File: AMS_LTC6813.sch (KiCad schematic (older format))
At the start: 69 parts, among them J1 CELLVOLCON, J10 Conn_01x02_Male, J11 Conn_01x02_Male, J12 Conn_01x02_Male, J13 Conn_01x02_Male, J14 Conn_01x02_Male, J15 Conn_01x02_Male, J16 Conn_01x02_Male, J17 Conn_01x02_Male, J18 Conn_01x02_Male, J19 Conn_01x02_Male, J2 TEMPSENCON, J20 Conn_01x02_Male, J21 Conn_01x02_Male, J22 Conn_01x02_Male, J23 Conn_01x02_Male, J24 Conn_01x02_Male, J25 Conn_01x02_Male, J26 Conn_01x02_Male, J27 Conn_01x02_Male, J28 Conn_01x02_Male, J29 Conn_01x02_Male, J3 ISOSPI2, J30 Conn_01x02_Male, J31 Conn_01x02_Male, J32 Conn_01x02_Male, J33 Conn_01x02_Male, J34 Conn_01x02_Male, J35 Conn_01x02_Male, J36 Conn_01x02_Male, J37 Conn_01x02_Male, J38 Conn_01x02_Male, J39 Conn_01x02_Male, J4 ISOSPI1, J40 Conn_01x02_Male, J41 Conn_01x02_Male, J42 Conn_01x02_Male, J43 Conn_01x02_Male, J44 Conn_01x02_Male, J45 Conn_01x02_Male, J46 Conn_01x02_Male, J47 Conn_01x02_Male, J48 Conn_01x02_Male, J49 Conn_01x02_Male, J5 Conn_01x02_Male, J50 Conn_01x02_Male, J51 Conn_01x02_Male, J52 Conn_01x02_Male, J53 Conn_01x02_Male, J54 Conn_01x02_Male, J55 Conn_01x02_Male, J56 Conn_01x02_Male, J57 Conn_01x02_Male, J58 Conn_01x02_Male, J59 Conn_01x02_Male, J6 Conn_01x02_Male, J60 Conn_01x02_Male, J61 Conn_01x02_Male, J62 Conn_01x02_Male, J63 Conn_01x02_Male, J64 Conn_01x02_Male, J65 Conn_01x02_Male, J66 Conn_01x02_Male, J67 Conn_01x02_Male, J68 Conn_01x02_Male, J7 Conn_01x02_Male, J8 Conn_01x02_Male, J9 Conn_01x02_Male, U2 LTC6813-1

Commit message: adding com
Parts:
- removed J1: CELLVOLCON, AMS_custom_lib:VOLCELLCON, symbol AMS_custom_lib:CELLVOLCON
- removed J2: TEMPSENCON, AMS_custom_lib:TEMPSENSCON, symbol AMS_custom_lib:TEMPSENCON
- removed J3: ISOSPI2, AMS_custom_lib:ISOSPICON, symbol AMS_custom_lib:ISOSPI2
- removed J4: ISOSPI1, AMS_custom_lib:ISOSPICON, symbol AMS_custom_lib:ISOSPI1
- added J?: Conn_02x20_Counter_Clockwise, Connector_IDC:IDC-Header_2x20_P2.54mm_Vertical, symbol Connector_Generic:Conn_02x20_Counter_Clockwise
- added J? (x2): Conn_01x03_Female, Connector_PinHeader_2.54mm:PinHeader_1x03_P2.54mm_Vertical, symbol Connector:Conn_01x03_Female
- added J? (x2): Conn_01x06, Connector_PinHeader_2.54mm:PinHeader_1x06_P2.54mm_Vertical, symbol Connector_Generic:Conn_01x06
- added J? (x2): Conn_02x02_Counter_Clockwise, Connector_PinHeader_2.54mm:PinHeader_2x02_P2.54mm_Vertical, symbol Connector_Generic:Conn_02x02_Counter_Clockwise
- added R?: 100, Resistor_SMD:R_1206_3216Metric_Pad1.42x1.75mm_HandSolder, symbol Device:R
- added R?: 5k, Resistor_SMD:R_1206_3216Metric_Pad1.42x1.75mm_HandSolder, symbol Device:R
- added U?: LTC6820, Package_SO:MSOP-16_3x4mm_P0.5mm, symbol AMS_custom_lib:LTC6820
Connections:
- net V- is gone; now on net C0: J63.1 (Pin_1), J63.2 (Pin_2), J64.1 (Pin_1), J64.2 (Pin_2), U2.59 (V-), U2.60 (V-)
- net C0: now also J?.2 (Pin_2), J?.20 (Pin_20), J?.3 (Pin_3), J?.5 (Pin_5), U?.14 (GND)
- net CELL1: now also J?.19 (Pin_19)
- net CELL10: now also J?.10 (Pin_10)
- net CELL11: now also J?.9 (Pin_9)
- net CELL12: now also J?.8 (Pin_8)
- net CELL2: now also J?.18 (Pin_18)
- net CELL3: now also J?.17 (Pin_17)
- net CELL4: now also J?.16 (Pin_16)
- net CELL5: now also J?.15 (Pin_15)
- net CELL6: now also J?.14 (Pin_14)
- net CELL7: now also J?.13 (Pin_13)
- net CELL8: now also J?.12 (Pin_12)
- net CELL9: now also J?.11 (Pin_11)
- net CSBIMA: now also J?.2 (Pin_2), J?.2 (Pin_2)
- net GPIO1: now also J?.21 (Pin_21)
- net GPIO2: now also J?.22 (Pin_22)
- net GPIO3: now also J?.23 (Pin_23)
- net GPIO4: now also J?.24 (Pin_24)
- net GPIO5: now also J?.25 (Pin_25)
- net GPIO6: now also J?.26 (Pin_26)
- net GPIO7: now also J?.27 (Pin_27)
- net GPIO8: now also J?.28 (Pin_28)
- net GPIO9: now also J?.29 (Pin_29)
- net IBIAS: now also J?.1 (Pin_1)
- net IMB: now also R?.1
- net IPB: now also R?.2
- net SCKIPA: now also J?.1 (Pin_1), J?.1 (Pin_1)
- net SDI: now also J?.4 (Pin_4)
- net SDO: now also J?.3 (Pin_3), R?.1
- new net CELL13: J?.7 (Pin_7)
- new net CELL14: J?.6 (Pin_6)
- new net CELL15: J?.5 (Pin_5)
- new net CELL16: J?.4 (Pin_4)
- new net CELL17: J?.3 (Pin_3)
- new net CELL18: J?.2 (Pin_2)
- new net CS: J?.5 (Pin_5), U?.5 (~CS)
- new net CSBIMA1: J?.2 (Pin_2), J?.3 (Pin_3)
- new net GND1: J?.3 (Pin_3)
- new net IBIAS1: J?.1 (Pin_1), U?.16 (IBIAS)
- new net ICMB: J?.2 (Pin_2)
- new net ICMB1: J?.2 (Pin_2)
- new net ICMP1: U?.15 (ICMP)
- new net IM: J?.3 (Pin_3), U?.10 (IM)
- new net IP: J?.4 (Pin_4), U?.11 (ID)
- new net MISO: J?.4 (Pin_4), U?.3 (MISO)
- new net MOSI: J?.3 (Pin_3), U?.2 (MOSI)
- new net SCK: U?.4 (SCK)
- new net SCKIPA1: J?.1 (Pin_1), J?.4 (Pin_4)
- new net SCk: J?.6 (Pin_6)
- new net VDD1: J?.1 (Pin_1), U?.12 (MSTR), U?.6 (Vdds), U?.7 (POL), U?.8 (PMD), U?.9 (Vdd)
- new net VDD2: J?.6 (Pin_6), R?.2

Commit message: blabl
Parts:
- added C? (x3): 1u, Capacitor_SMD:C_1210_3225Metric_Pad1.42x2.65mm_HandSolder, symbol Device:C
- added C?: 0.1u, Capacitor_SMD:C_1210_3225Metric_Pad1.42x2.65mm_HandSolder, symbol Device:C
- added Q?: 2N2219, Package_TO_SOT_THT:TO-39-3, symbol Transistor_BJT:2N2219
- added R?: R, Resistor_SMD:R_1206_3216Metric_Pad1.42x1.75mm_HandSolder, symbol Device:R
- gave numbers to parts that had none: 10
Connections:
- net C0: now also C?.2, C?.2, C?.2, C?.2
- net C18: now also R?.1
- net DRIVE: now also Q?.2 (B)
- net VREF1: now also C?.1
- net VREF2: now also C?.1
- net VREG: now also C?.1, Q?.1 (E)
- new net C: C?.1, Q?.3 (C), R?.2
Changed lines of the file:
@@
 CELL18
 $Comp
-L Connector_Generic:Conn_02x20_Counter_Clockwise J?
+L Connector_Generic:Conn_02x20_Counter_Clockwise J71
 U 1 1 5F95EEEE
 P 9400 1700
-F 0 "J?" H 9450 2817 50  0000 C CNN
+F 0 "J71" H 9450 2817 50  0000 C CNN
 F 1 "Conn_02x20_Counter_Clockwise" H 9450 2726 50  0000 C CNN
 F 2 "Connector_IDC:IDC-Header_2x20_P2.54mm_Vertical" H 9400 1700 50  0001 C CNN
@@
 GPIO9
 $Comp
-L Device:R R?
+L Device:R R73
 U 1 1 5F96165A
 P 4600 6250
-F 0 "R?" V 4393 6250 50  0000 C CNN
+F 0 "R73" V 4393 6250 50  0000 C CNN
 F 1 "100" V 4484 6250 50  0000 C CNN
 F 2 "Resistor_SMD:R_1206_3216Metric_Pad1.42x1.75mm_HandSolder" V 4530 6250 50  0001 C CNN
@@
 CSBIMA1
 $Comp
-L Connector_Generic:Conn_01x06 J?
+L Connector_Generic:Conn_01x06 J3
 U 1 1 5F963338
 P 5850 5200
-F 0 "J?" H 5930 5192 50  0000 L CNN
+F 0 "J3" H 5930 5192 50  0000 L CNN
 F 1 "Conn_01x06" H 5930 5101 50  0000 L CNN
 F 2 "Connector_PinHeader_2.54mm:PinHeader_1x06_P2.54mm_Vertical" H 5850 5200 50  0001 C CNN
@@
 VDD2
 $Comp
-L Device:R R?
+L Device:R R74
 U 1 1 5F963D26
 P 5350 5350
-F 0 "R?" H 5420 5396 50  0000 L CNN
+F 0 "R74" H 5420 5396 50  0000 L CNN
 F 1 "5k" H 5420 5305 50  0000 L CNN
 F 2 "Resistor_SMD:R_1206_3216Metric_Pad1.42x1.75mm_HandSolder" V 5280 5350 50  0001 C CNN
@@
 Connection ~ 5350 5500
 $Comp
-L AMS_custom_lib:LTC6820 U?
+L AMS_custom_lib:LTC6820 U1
 U 1 1 5F9642E1
 P 6000 7000
-F 0 "U?" H 5975 7615 50  0000 C CNN
+F 0 "U1" H 5975 7615 50  0000 C CNN
 F 1 "LTC6820" H 5975 7524 50  0000 C CNN
 F 2 "Package_SO:MSOP-16_3x4mm_P0.5mm" H 5950 7500 50  0001 C CNN
@@
 $EndComp
 $Comp
-L Connector_Generic:Conn_01x06 J?
+L Connector_Generic:Conn_01x06 J1
 U 1 1 5F9647DF
 P 4550 7050
-F 0 "J?" H 4470 6525 50  0000 C CNN
+F 0 "J1" H 4470 6525 50  0000 C CNN
 F 1 "Conn_01x06" H 4470 6616 50  0000 C CNN
 F 2 "Connector_PinHeader_2.54mm:PinHeader_1x06_P2.54mm_Vertical" H 4550 7050 50  0001 C CNN
@@
 VDD1
 $Comp
-L Connector_Generic:Conn_02x02_Counter_Clockwise J?
+L Connector_Generic:Conn_02x02_Counter_Clockwise J69
 U 1 1 5F96687F
 P 7100 5300
-F 0 "J?" H 7150 5517 50  0000 C CNN
+F 0 "J69" H 7150 5517 50  0000 C CNN
 F 1 "Conn_02x02_Counter_Clockwise" H 7150 5426 50  0000 C CNN
 F 2 "Connector_PinHeader_2.54mm:PinHeader_2x02_P2.54mm_Vertical" H 7100 5300 50  0001 C CNN
@@
 CSBIMA
 $Comp
-L Connector_Generic:Conn_02x02_Counter_Clockwise J?
+L Connector_Generic:Conn_02x02_Counter_Clockwise J4
 U 1 1 5F967148
 P 6450 6000
-F 0 "J?" H 6500 6217 50  0000 C CNN
+F 0 "J4" H 6500 6217 50  0000 C CNN
 F 1 "Conn_02x02_Counter_Clockwise" H 6500 6126 50  0000 C CNN
 F 2 "Connector_PinHeader_2.54mm:PinHeader_2x02_P2.54mm_Vertical" H 6450 6000 50  0001 C CNN
@@
 GND
 $Comp
-L Connector:Conn_01x03_Female J?
+L Connector:Conn_01x03_Female J2
 U 1 1 5F962EA3
 P 4750 5650
-F 0 "J?" H 4777 5676 50  0000 L CNN
+F 0 "J2" H 4777 5676 50  0000 L CNN
 F 1 "Conn_01x03_Female" H 4777 5585 50  0000 L CNN
 F 2 "Connector_PinHeader_2.54mm:PinHeader_1x03_P2.54mm_Vertical" H 4750 5650 50  0001 C CNN
@@
 $EndComp
 $Comp
-L Connector:Conn_01x03_Female J?
+L Connector:Conn_01x03_Female J70
 U 1 1 5F9677A5
 P 7550 6000
-F 0 "J?" H 7577 6026 50  0000 L CNN
+F 0 "J70" H 7577 6026 50  0000 L CNN
 F 1 "Conn_01x03_Female" H 7577 5935 50  0000 L CNN
 F 2 "Connector_PinHeader_2.54mm:PinHeader_1x03_P2.54mm_Vertical" H 7550 6000 50  0001 C CNN
@@
 Text Label 5550 7350 2    50   ~ 0
 VDD1
+$Comp
+L Device:C C?
+U 1 1 5F96A5E9
+P 9150 5150
+F 0 "C?" H 9265 5196 50  0000 L CNN
+F 1 "1u" H 9265 5105 50  0000 L CNN
+F 2 "Capacitor_SMD:C_1210_3225Metric_Pad1.42x2.65mm_HandSolder" H 9188 5000 50  0001 C CNN
+F 3 "~" H 9150 5150 50  0001 C CNN
+	1    9150 5150
+	1    0    0    -1
+$EndComp
+$Comp
+L Device:C C?
+U 1 1 5F96A6FB
+P 9500 5150
+F 0 "C?" H 9615 5196 50  0000 L CNN
+F 1 "1u" H 9615 5105 50  0000 L CNN
+F 2 "Capacitor_SMD:C_1210_3225Metric_Pad1.42x2.65mm_HandSolder" H 9538 5000 50  0001 C CNN
+F 3 "~" H 9500 5150 50  0001 C CNN
+	1    9500 5150
+	1    0    0    -1
+$EndComp
+$Comp
+L Device:C C?
+U 1 1 5F96A94A
+P 9850 5150
+F 0 "C?" H 9965 5196 50  0000 L CNN
+F 1 "1u" H 9965 5105 50  0000 L CNN
+F 2 "Capacitor_SMD:C_1210_3225Metric_Pad1.42x2.65mm_HandSolder" H 9888 5000 50  0001 C CNN
+F 3 "~" H 9850 5150 50  0001 C CNN
+	1    9850 5150
+	1    0    0    -1
+$EndComp
+$Comp
+L Device:C C?
+U 1 1 5F96AA68
+P 10200 5150
+F 0 "C?" H 10315 5196 50  0000 L CNN
+F 1 "0.1u" H 10315 5105 50  0000 L CNN
+F 2 "Capacitor_SMD:C_1210_3225Metric_Pad1.42x2.65mm_HandSolder" H 10238 5000 50  0001 C CNN
+F 3 "~" H 10200 5150 50  0001 C CNN
+	1    10200 5150
+	1    0    0    -1
+$EndComp
+Text Label 10550 5300 0    50   ~ 0
+GND
+Wire Wire Line
+	10550 5300 10200 5300
+Wire Wire Line
+	10200 5300 9850 5300
+Connection ~ 10200 5300
+Wire Wire Line
+	9850 5300 9500 5300
+Connection ~ 9850 5300
+Wire Wire Line
+	9500 5300 9150 5300
+Connection ~ 9500 5300
+Text Label 9150 5000 0    50   ~ 0
+VREF1
+Text Label 9500 5000 0    50   ~ 0
+VREF2
+Text Label 9850 5000 0    50   ~ 0
+VREG
+$Comp
+L Device:R R?
+U 1 1 5F96B10A
+P 10200 4850
+F 0 "R?" H 10270 4896 50  0000 L CNN
+F 1 "R" H 10270 4805 50  0000 L CNN
+F 2 "Resistor_SMD:R_1206_3216Metric_Pad1.42x1.75mm_HandSolder" V 10130 4850 50  0001 C CNN
+F 3 "~" H 10200 4850 50  0001 C CNN
+	1    10200 4850
+	1    0    0    -1
+$EndComp
+Text Label 10200 4700 0    50   ~ 0
+C18
+Text Label 10200 5000 0    50   ~ 0
+C
+$Comp
+L Transistor_BJT:2N2219 Q?
+U 1 1 5F96B7EA
+P 9900 5900
+F 0 "Q?" H 10091 5946 50  0000 L CNN
+F 1 "2N2219" H 10091 5855 50  0000 L CNN
+F 2 "Package_TO_SOT_THT:TO-39-3" H 10100 5825 50  0001 L CIN
+F 3 "http://www.onsemi.com/pub_link/Collateral/2N2219-D.PDF" H 9900 5900 50  0001 L CNN
+	1    9900 5900
+	1    0    0    -1
+$EndComp
+Text Label 10000 5700 0    50   ~ 0
+C
+Text Label 10000 6100 0    50   ~ 0
+VREG
+Text Label 9700 5900 2    50   ~ 0
+DRIVE
 $EndSCHEMATC

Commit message: petite modif
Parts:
- added J72, J73, J74, J75, J76, J77, J78, J79, J80, J81, J82, J83, J84, J85, J86, J87: Conn_01x02_Male, Connector_PinHeader_2.54mm:PinHeader_1x02_P2.54mm_Vertical, symbol Connector:Conn_01x02_Male
- gave numbers to parts that had none: 6
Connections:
- net C0: now also J82.1 (Pin_1), J82.2 (Pin_2)
- net CS: now also J76.1 (Pin_1), J76.2 (Pin_2)
- net IBIAS1: now also J80.1 (Pin_1), J80.2 (Pin_2)
- net ICMP1: now also J81.1 (Pin_1), J81.2 (Pin_2)
- net IM: now also J86.1 (Pin_1), J86.2 (Pin_2)
- net IP: now also J85.1 (Pin_1), J85.2 (Pin_2)
- net MISO: now also J74.1 (Pin_1), J74.2 (Pin_2)
- net MOSI: now also J73.1 (Pin_1), J73.2 (Pin_2)
- net SCK: now also J75.1 (Pin_1), J75.2 (Pin_2)
- net VDD1: now also J77.1 (Pin_1), J77.2 (Pin_2), J78.1 (Pin_1), J78.2 (Pin_2), J79.1 (Pin_1), J79.2 (Pin_2), J84.1 (Pin_1), J84.2 (Pin_2), J87.1 (Pin_1), J87.2 (Pin_2)
- net EN: now reaches U1.1 (EN)
- net EN: now also J72.1 (Pin_1), J72.2 (Pin_2)
- net SLOW: now reaches U1.13 (SLOW)
- net SLOW: now also J83.1 (Pin_1), J83.2 (Pin_2)
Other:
- moved on the sheet: J1, J2, R73

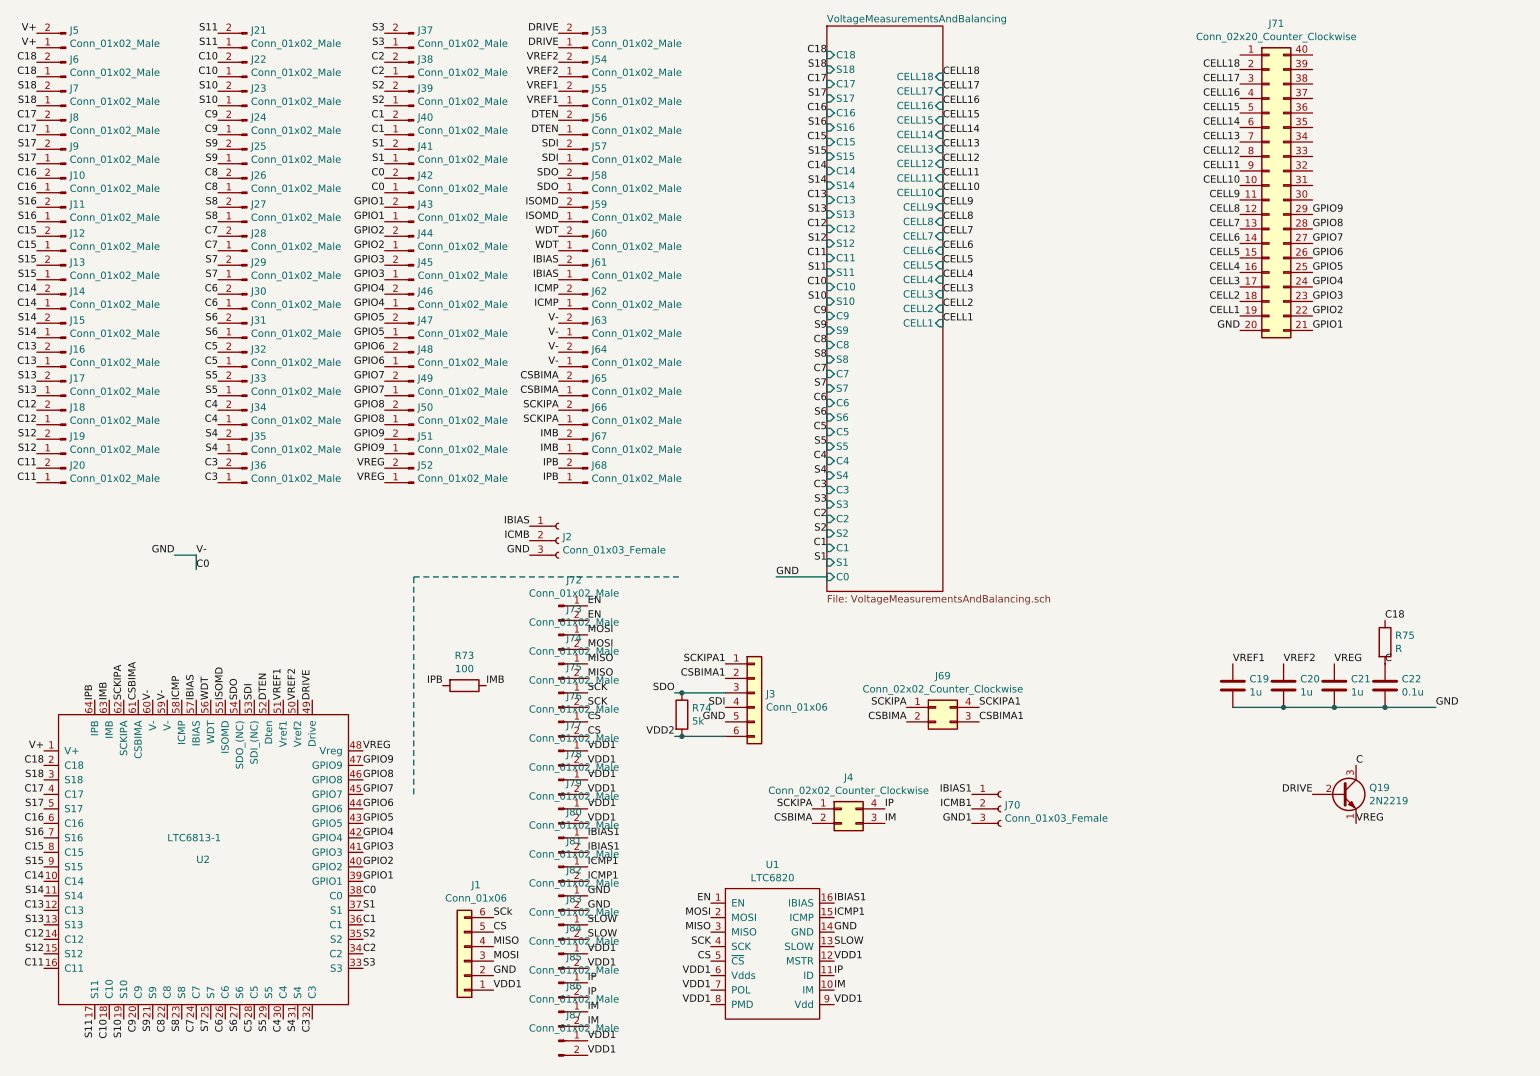
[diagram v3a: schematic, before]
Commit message: tout route sauf voltage channel
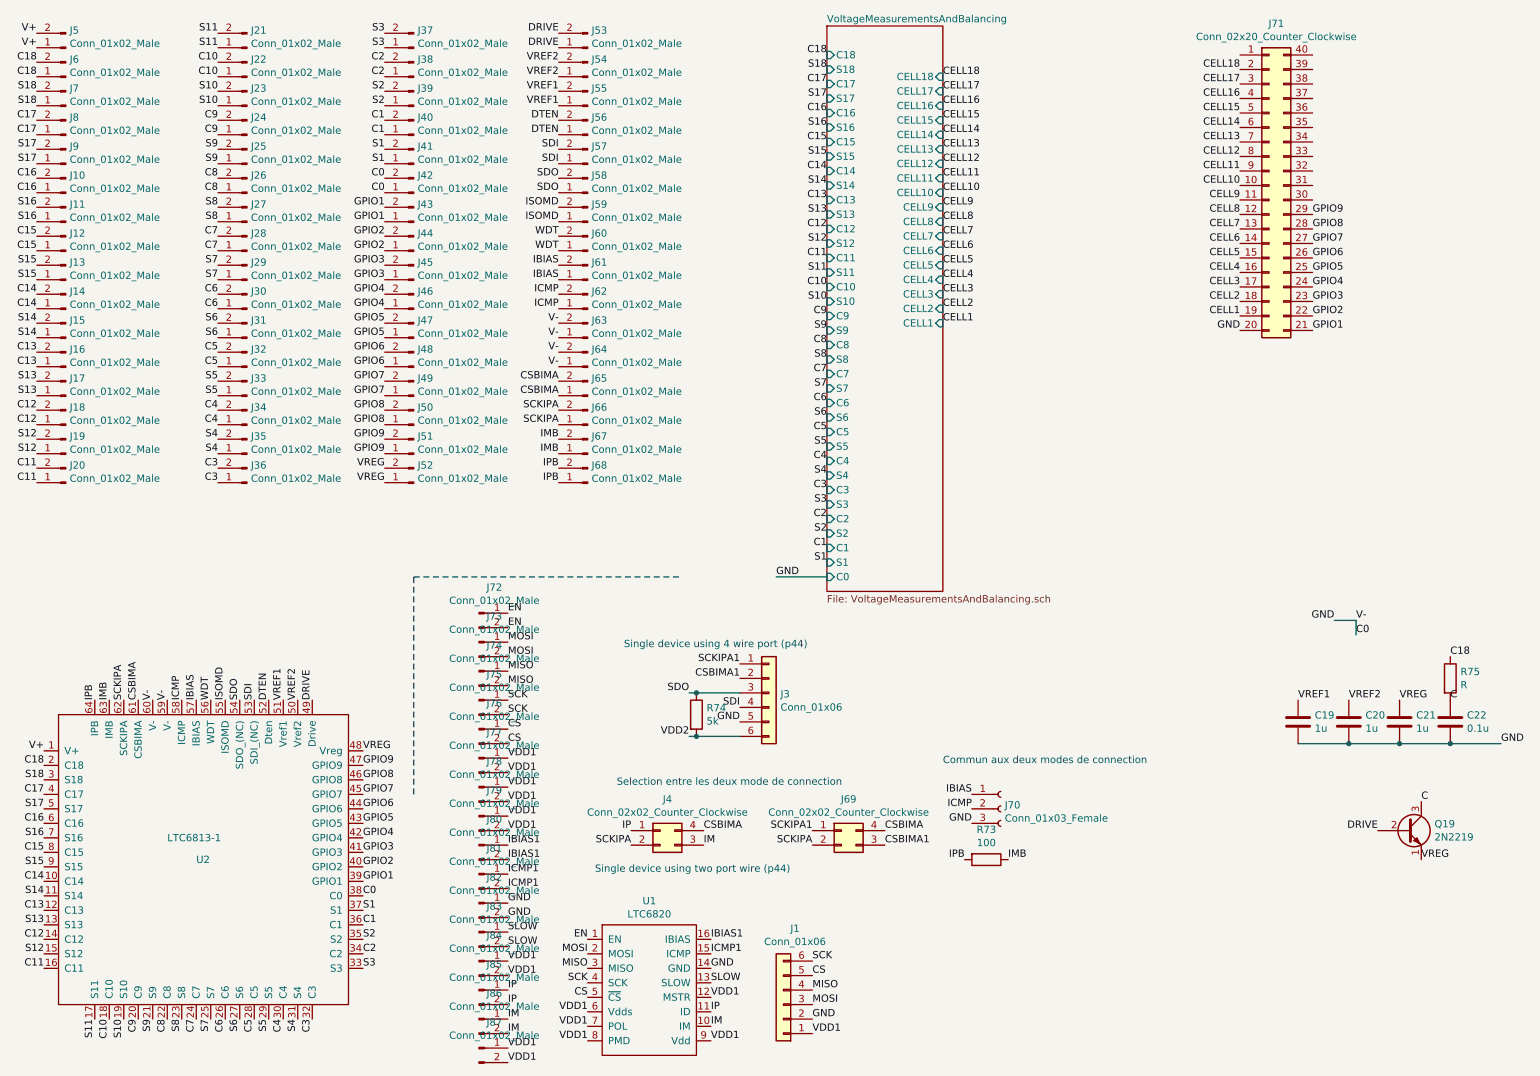
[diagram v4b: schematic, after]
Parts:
- removed J2: Conn_01x03_Female, Connector_PinHeader_2.54mm:PinHeader_1x03_P2.54mm_Vertical, symbol Connector:Conn_01x03_Female
- Q19: footprint Package_TO_SOT_THT:TO-39-3 -> Package_TO_SOT_SMD:SOT-223-3_TabPin2
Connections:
- net GND1 is gone; now on net C0: J70.3 (Pin_3)
- net ICMB1 is gone; now on net ICMP: J70.2 (Pin_2)
- net SCk is gone; now on net SCK: J1.6 (Pin_6)
- net CSBIMA: now also J4.4 (Pin_4), J69.4 (Pin_4); no longer J4.2 (Pin_2), J69.2 (Pin_2)
- net IBIAS: now also J70.1 (Pin_1)
- net IBIAS1: no longer J70.1 (Pin_1)
- net IP: now also J4.1 (Pin_1); no longer J4.4 (Pin_4)
- net SCKIPA: now also J4.2 (Pin_2), J69.2 (Pin_2); no longer J4.1 (Pin_1), J69.1 (Pin_1)
- net SCKIPA1: now also J69.1 (Pin_1); no longer J69.4 (Pin_4)
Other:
- note added: "Commun aux deux modes de connection"
- note added: "Selection entre les deux mode de connection\n"
- note added: "Single device using 4 wire port (p44)"
- note added: "Single device using two port wire (p44)"
- moved on the sheet: C19, C20, C21, C22, J1, J3, J4, J69, J72, J73, J74, J75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
